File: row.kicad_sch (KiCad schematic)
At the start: 16 parts

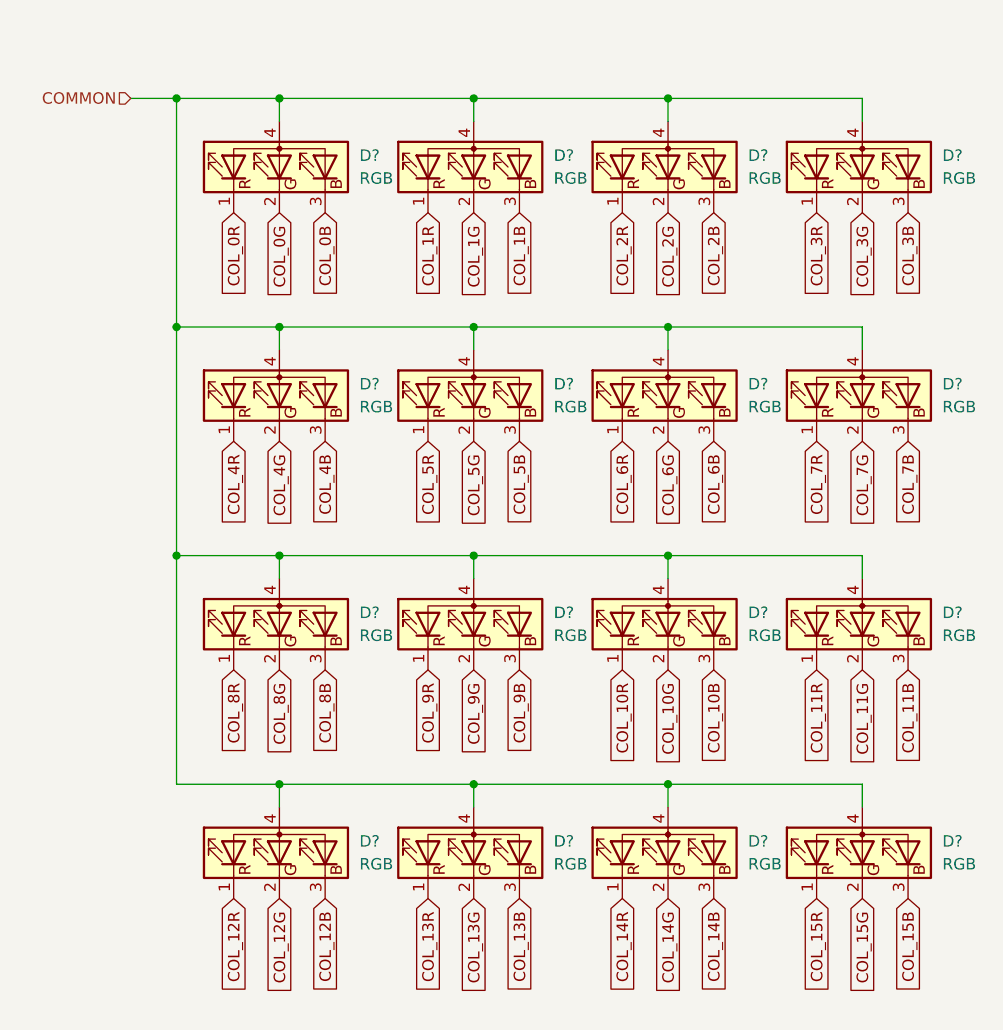
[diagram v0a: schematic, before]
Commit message: Row/column labels attached to shift registers/drivers
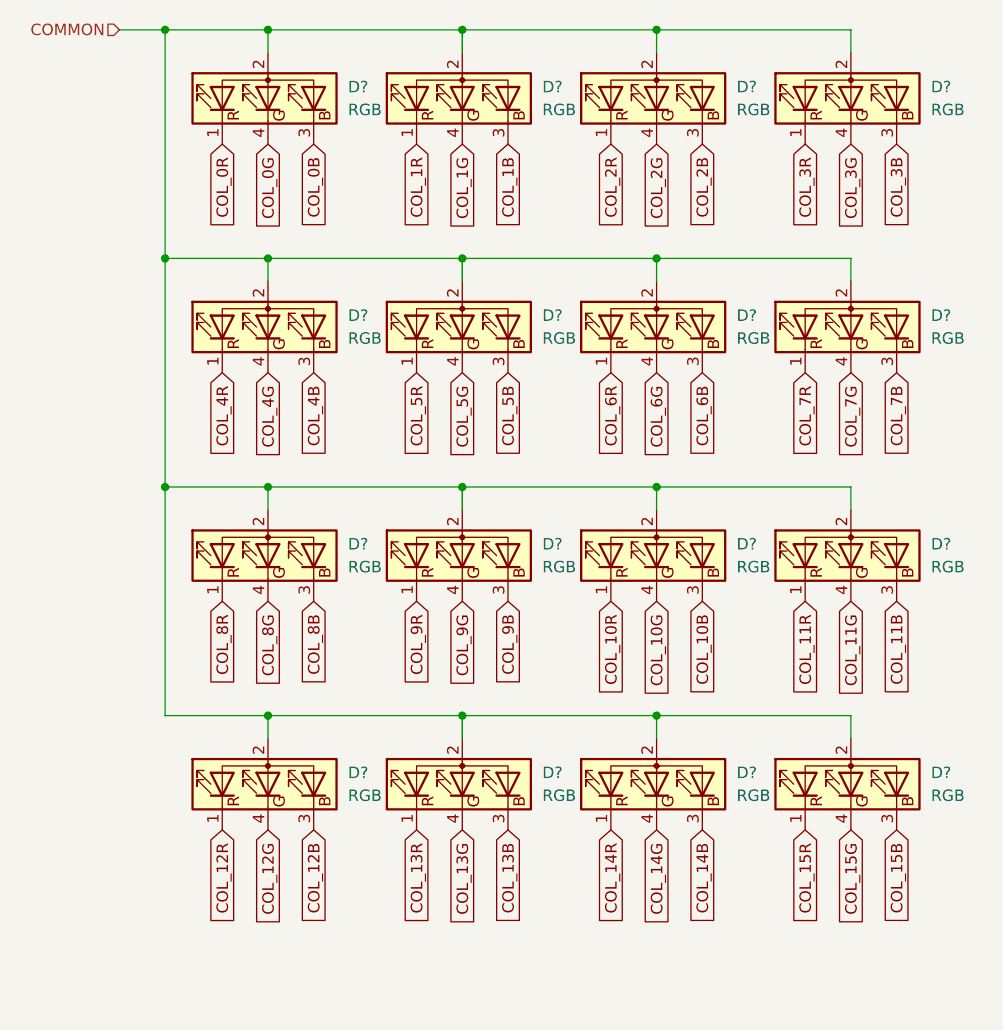
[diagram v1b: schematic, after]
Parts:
- D? (x16): symbol Device:LED_RGBA -> Device:LED_RABG
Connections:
- net COL_0G: now also D?.4 (GK); no longer D?.2 (GK)
- net COL_10G: now also D?.4 (GK); no longer D?.2 (GK)
- net COL_11G: now also D?.4 (GK); no longer D?.2 (GK)
- net COL_12G: now also D?.4 (GK); no longer D?.2 (GK)
- net COL_13G: now also D?.4 (GK); no longer D?.2 (GK)
- net COL_14G: now also D?.4 (GK); no longer D?.2 (GK)
- net COL_15G: now also D?.4 (GK); no longer D?.2 (GK)
- net COL_1G: now also D?.4 (GK); no longer D?.2 (GK)
- net COL_2G: now also D?.4 (GK); no longer D?.2 (GK)
- net COL_3G: now also D?.4 (GK); no longer D?.2 (GK)
- net COL_4G: now also D?.4 (GK); no longer D?.2 (GK)
- net COL_5G: now also D?.4 (GK); no longer D?.2 (GK)
- net COL_6G: now also D?.4 (GK); no longer D?.2 (GK)
- net COL_7G: now also D?.4 (GK); no longer D?.2 (GK)
- net COL_8G: now also D?.4 (GK); no longer D?.2 (GK)
- net COL_9G: now also D?.4 (GK); no longer D?.2 (GK)
- net COMMON: now also D?.2 (A), D?.2 (A), D?.2 (A), D?.2 (A), D?.2 (A), D?.2 (A), D?.2 (A), D?.2 (A), D?.2 (A), D?.2 (A), D?.2 (A), D?.2 (A), D?.2 (A), D?.2 (A), D?.2 (A), D?.2 (A); no longer D?.4 (A), D?.4 (A), D?.4 (A), D?.4 (A), D?.4 (A), D?.4 (A), D?.4 (A), D?.4 (A), D?.4 (A), D?.4 (A), D?.4 (A), D?.4 (A), D?.4 (A), D?.4 (A), D?.4 (A), D?.4 (A)
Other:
- moved on the sheet: D?

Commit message: PMOS drivers, buffers, and serial connections
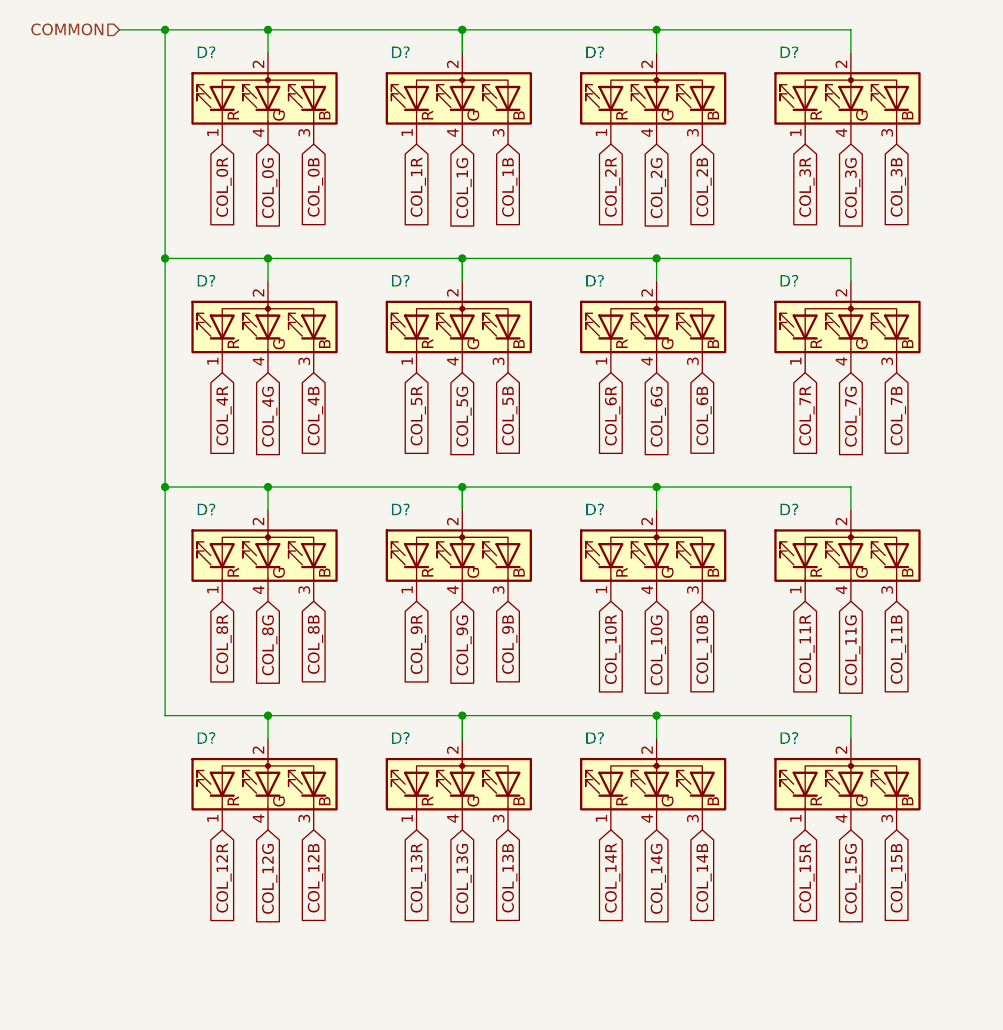
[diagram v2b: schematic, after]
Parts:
- removed D? (x15): RGB, symbol Device:LED_RABG
- added D? (x15): LED_RABG, symbol Device:LED_RABG
- D?: value RGB -> LED_RABG
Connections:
- net COL_10B: now also D?.3 (BK)
- net COL_10G: now also D?.4 (GK)
- net COL_10R: now also D?.1 (RK)
- net COL_11B: now also D?.3 (BK)
- net COL_11G: now also D?.4 (GK)
- net COL_11R: now also D?.1 (RK)
- net COL_12B: now also D?.3 (BK)
- net COL_12G: now also D?.4 (GK)
- net COL_12R: now also D?.1 (RK)
- net COL_13B: now also D?.3 (BK)
- net COL_13G: now also D?.4 (GK)
- net COL_13R: now also D?.1 (RK)
- net COL_14B: now also D?.3 (BK)
- net COL_14G: now also D?.4 (GK)
- net COL_14R: now also D?.1 (RK)
- net COL_15B: now also D?.3 (BK)
- net COL_15G: now also D?.4 (GK)
- net COL_15R: now also D?.1 (RK)
- net COL_1B: now also D?.3 (BK)
- net COL_1G: now also D?.4 (GK)
- net COL_1R: now also D?.1 (RK)
- net COL_2B: now also D?.3 (BK)
- net COL_2G: now also D?.4 (GK)
- net COL_2R: now also D?.1 (RK)
- net COL_3B: now also D?.3 (BK)
- net COL_3G: now also D?.4 (GK)
- net COL_3R: now also D?.1 (RK)
- net COL_4B: now also D?.3 (BK)
- net COL_4G: now also D?.4 (GK)
- net COL_4R: now also D?.1 (RK)
- net COL_5B: now also D?.3 (BK)
- net COL_5G: now also D?.4 (GK)
- net COL_5R: now also D?.1 (RK)
- net COL_6B: now also D?.3 (BK)
- net COL_6G: now also D?.4 (GK)
- net COL_6R: now also D?.1 (RK)
- net COL_7B: now also D?.3 (BK)
- net COL_7G: now also D?.4 (GK)
- net COL_7R: now also D?.1 (RK)
- net COL_8B: now also D?.3 (BK)
- net COL_8G: now also D?.4 (GK)
- net COL_8R: now also D?.1 (RK)
- net COL_9B: now also D?.3 (BK)
- net COL_9G: now also D?.4 (GK)
- net COL_9R: now also D?.1 (RK)
- net COMMON: now also D?.2 (A), D?.2 (A), D?.2 (A), D?.2 (A), D?.2 (A), D?.2 (A), D?.2 (A), D?.2 (A), D?.2 (A), D?.2 (A), D?.2 (A), D?.2 (A), D?.2 (A), D?.2 (A), D?.2 (A)

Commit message: LED footprint
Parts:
- D? (x16): footprint (none) -> ledcube:MHPA1515RGBDT
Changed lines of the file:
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@@
       (effects (font (size 1.27 1.27)) hide)
     )
-    (property "Footprint" "" (id 2) (at 114.3 58.42 0)
+    (property "Footprint" "ledcube:MHPA1515RGBDT" (id 2) (at 114.3 58.42 0)
       (effects (font (size 1.27 1.27)) hide)
     )
@@
       (effects (font (size 1.27 1.27)) hide)
     )
-    (property "Footprint" "" (id 2) (at 114.3 83.82 0)
+    (property "Footprint" "ledcube:MHPA1515RGBDT" (id 2) (at 114.3 83.82 0)
       (effects (font (size 1.27 1.27)) hide)
     )
@@
       (effects (font (size 1.27 1.27)) hide)
     )
-    (property "Footprint" "" (id 2) (at 114.3 109.22 0)
+    (property "Footprint" "ledcube:MHPA1515RGBDT" (id 2) (at 114.3 109.22 0)
       (effects (font (size 1.27 1.27)) hide)
     )
@@
       (effects (font (size 1.27 1.27)) hide)
     )
-    (property "Footprint" "" (id 2) (at 114.3 134.62 0)
+    (property "Footprint" "ledcube:MHPA1515RGBDT" (id 2) (at 114.3 134.62 0)
       (effects (font (size 1.27 1.27)) hide)
     )
@@
       (effects (font (size 1.27 1.27)) hide)
     )
-    (property "Footprint" "" (id 2) (at 135.89 58.42 0)
+    (property "Footprint" "ledcube:MHPA1515RGBDT" (id 2) (at 135.89 58.42 0)
       (effects (font (size 1.27 1.27)) hide)
     )
@@
       (effects (font (size 1.27 1.27)) hide)
     )
-    (property "Footprint" "" (id 2) (at 135.89 83.82 0)
+    (property "Footprint" "ledcube:MHPA1515RGBDT" (id 2) (at 135.89 83.82 0)
       (effects (font (size 1.27 1.27)) hide)
     )
@@
       (effects (font (size 1.27 1.27)) hide)
     )
-    (property "Footprint" "" (id 2) (at 135.89 109.22 0)
+    (property "Footprint" "ledcube:MHPA1515RGBDT" (id 2) (at 135.89 109.22 0)
       (effects (font (size 1.27 1.27)) hide)
     )
@@
       (effects (font (size 1.27 1.27)) hide)
     )
-    (property "Footprint" "" (id 2) (at 135.89 134.62 0)
+    (property "Footprint" "ledcube:MHPA1515RGBDT" (id 2) (at 135.89 134.62 0)
       (effects (font (size 1.27 1.27)) hide)
     )
@@
       (effects (font (size 1.27 1.27)) hide)
     )
-    (property "Footprint" "" (id 2) (at 157.48 58.42 0)
+    (property "Footprint" "ledcube:MHPA1515RGBDT" (id 2) (at 157.48 58.42 0)
       (effects (font (size 1.27 1.27)) hide)
     )
@@
       (effects (font (size 1.27 1.27)) hide)
     )
-    (property "Footprint" "" (id 2) (at 157.48 83.82 0)
+    (property "Footprint" "ledcube:MHPA1515RGBDT" (id 2) (at 157.48 83.82 0)
       (effects (font (size 1.27 1.27)) hide)
     )
@@
       (effects (font (size 1.27 1.27)) hide)
     )
-    (property "Footprint" "" (id 2) (at 157.48 109.22 0)
+    (property "Footprint" "ledcube:MHPA1515RGBDT" (id 2) (at 157.48 109.22 0)
       (effects (font (size 1.27 1.27)) hide)
     )
@@
       (effects (font (size 1.27 1.27)) hide)
     )
-    (property "Footprint" "" (id 2) (at 157.48 134.62 0)
+    (property "Footprint" "ledcube:MHPA1515RGBDT" (id 2) (at 157.48 134.62 0)
       (effects (font (size 1.27 1.27)) hide)
     )
@@
       (effects (font (size 1.27 1.27)) hide)
     )
-    (property "Footprint" "" (id 2) (at 179.07 58.42 0)
+    (property "Footprint" "ledcube:MHPA1515RGBDT" (id 2) (at 179.07 58.42 0)
       (effects (font (size 1.27 1.27)) hide)
     )
@@
       (effects (font (size 1.27 1.27)) hide)
     )
-    (property "Footprint" "" (id 2) (at 179.07 83.82 0)
+    (property "Footprint" "ledcube:MHPA1515RGBDT" (id 2) (at 179.07 83.82 0)
       (effects (font (size 1.27 1.27)) hide)
     )
@@
       (effects (font (size 1.27 1.27)) hide)
     )
-    (property "Footprint" "" (id 2) (at 179.07 109.22 0)
+    (property "Footprint" "ledcube:MHPA1515RGBDT" (id 2) (at 179.07 109.22 0)
       (effects (font (size 1.27 1.27)) hide)
     )
@@
       (effects (font (size 1.27 1.27)) hide)
     )
-    (property "Footprint" "" (id 2) (at 179.07 134.62 0)
-      (effects (font (size 1.27 1.27)) hide)
-    )
+    (property "Footprint" "ledcube:MHPA1515RGBDT" (id 2) (at 179.07 134.62 0)
+      (effects (font (size 1.27 1.27)) hide)
+    )
